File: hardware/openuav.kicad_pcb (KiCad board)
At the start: 4 copper layers, 36 x 36 mm, 80 parts, among them J1 Conn_01x01, J10 Conn_01x01, J11 Conn_01x01, J12 Conn_01x01, J13 Conn_01x01, J14 Conn_01x01, J15 Conn_01x01, J16 Conn_01x01, J17 Conn_01x01, J18 Conn_01x01, J19 Conn_01x01, J2 Conn_01x01, J20 Conn_01x01, J21 Conn_01x01, J22 Conn_01x01, J23 Conn_01x01, J24 Conn_01x01, J25 Conn_01x01, J3 Conn_01x01, J4 Conn_01x01, J5 Conn_01x01, J6 Conn_01x01, J7 Conn_01x01, J8 Conn_01x01, J9 Conn_01x01, J99 USB_C_Receptacle_USB2.0, SW1 SW_Push, U1 STM32G431CBUx, U2 LPS22HH, U3 LSM6DSR, U4 TPS54302, U5 TLV75733PDBV, U6 W25N01GVZEIG, U7 TLV75733PDBV

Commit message: Change IMU to ICM-42688-P. Change top and bottom planes to GND.
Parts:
- U3: value LSM6DSR -> ICM-42688-P
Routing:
- net GND: vias 51 -> 60
- added copper zone on B.Cu, net GND
- removed copper zone on B.Cu, net (none)
- removed copper zone on F.Cu, net (none)
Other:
- board text added: "OPENUAV v0.4"
- board text removed: "OPENUAV v0.3"
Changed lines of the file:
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@@
     (descr "LGA, 14 Pin (https://www.st.com/resource/en/datasheet/lsm6ds3tr-c.pdf), generated with kicad-footprint-generator ipc_noLead_generator.py")
     (tags "LGA NoLead")
-    (property "LCSC" "C784817")
+    (property "LCSC" "C1850418")
     (property "Sheetfile" "openuav.kicad_sch")
     (property "Sheetname" "")
@@
         (effects (font (size 1 1) (thickness 0.15)))
     )
-    (fp_text value "LSM6DSR" (at 39 -1) (layer "F.Fab")
+    (fp_text value "ICM-42688-P" (at 39 -1) (layer "F.Fab")
         (effects (font (size 1 1) (thickness 0.15)))
     )
@@
   (gr_arc locked (start 165 50) (mid 165.707107 50.292893) (end 166 51)
     (stroke (width 0.2) (type default)) (layer "Edge.Cuts"))
-  (gr_text "OPENUAV v0.3" (at 160 55) (layer "B.SilkS")
+  (gr_text "OPENUAV v0.4" (at 160.1 52.3) (layer "B.SilkS")
     (effects (font (size 1 1) (thickness 0.2) bold) (justify left bottom mirror))
   )
-  (gr_text "JLCJLCJLCJLC" (at 146 83) (layer "B.SilkS")
+  (gr_text "JLCJLCJLCJLC" (at 146.7 84.7) (layer "B.SilkS")
     (effects (font (size 1 1) (thickness 0.2) bold) (justify left bottom mirror))
   )
-  (gr_text "DFU" (at 132.9 79.1) (layer "F.SilkS")
+  (gr_text "DFU" (at 136 76.55 -90) (layer "F.SilkS")
     (effects (font (size 1 1) (thickness 0.2) bold))
   )
@@
   (via (at 152.522738 70.493202) (size 0.5) (drill 0.3) (layers "F.Cu" "B.Cu") (net 1))
   (via (at 142.9 72.7) (size 0.5) (drill 0.3) (layers "F.Cu" "B.Cu") (net 1))
+  (via (at 151.2 55.8) (size 0.5) (drill 0.3) (layers "F.Cu" "B.Cu") (free) (net 1))
   (via (at 152 76.4) (size 0.5) (drill 0.3) (layers "F.Cu" "B.Cu") (net 1))
+  (via (at 141.6 56.2) (size 0.5) (drill 0.3) (layers "F.Cu" "B.Cu") (free) (net 1))
+  (via (at 132.9 77.4) (size 0.5) (drill 0.3) (layers "F.Cu" "B.Cu") (free) (net 1))
   (via (at 137.523 61.1) (size 0.5) (drill 0.3) (layers "F.Cu" "B.Cu") (free) (net 1))
   (via (at 134.7 57.5) (size 0.5) (drill 0.3) (layers "F.Cu" "B.Cu") (net 1))
+  (via (at 142.6 77.3) (size 0.5) (drill 0.3) (layers "F.Cu" "B.Cu") (free) (net 1))
   (via (at 163.1 76.7) (size 0.5) (drill 0.3) (layers "F.Cu" "B.Cu") (net 1))
   (via (at 151.022738 70.493202) (size 0.5) (drill 0.3) (layers "F.Cu" "B.Cu") (net 1))
+  (via (at 164.7 67.9) (size 0.5) (drill 0.3) (layers "F.Cu" "B.Cu") (free) (net 1))
   (via (at 138.4 77) (size 0.5) (drill 0.3) (layers "F.Cu" "B.Cu") (net 1))
   (via (at 139.523 61.1) (size 0.5) (drill 0.3) (layers "F.Cu" "B.Cu") (free) (net 1))
   (via (at 138 53.4) (size 0.5) (drill 0.3) (layers "F.Cu" "B.Cu") (net 1))
+  (via (at 159.8 52.4) (size 0.5) (drill 0.3) (layers "F.Cu" "B.Cu") (free) (net 1))
   (via (at 151.922738 75.393202) (size 0.5) (drill 0.3) (layers "F.Cu" "B.Cu") (net 1))
   (via (at 153.222738 75.393202) (size 0.5) (drill 0.3) (layers "F.Cu" "B.Cu") (net 1))
   (via (at 151.022738 67.493202) (size 0.5) (drill 0.3) (layers "F.Cu" "B.Cu") (net 1))
+  (via (at 143.2 79.8) (size 0.5) (drill 0.3) (layers "F.Cu" "B.Cu") (free) (net 1))
   (via (at 152.522738 68.993202) (size 0.5) (drill 0.3) (layers "F.Cu" "B.Cu") (net 1))
   (via (at 149.522738 68.993202) (size 0.5) (drill 0.3) (layers "F.Cu" "B.Cu") (net 1))
@@
   (via (at 158 82.6) (size 0.5) (drill 0.3) (layers "F.Cu" "B.Cu") (net 1))
   (via (at 148 53.4) (size 0.5) (drill 0.3) (layers "F.Cu" "B.Cu") (net 1))
+  (via (at 154.3 80.5) (size 0.5) (drill 0.3) (layers "F.Cu" "B.Cu") (free) (net 1))
   (via (at 138.523 61.1) (size 0.5) (drill 0.3) (layers "F.Cu" "B.Cu") (free) (net 1))
   (via (at 138.5 81.3) (size 0.5) (drill 0.3) (layers "F.Cu" "B.Cu") (net 1))
@@
   (via (at 145.3 67.395) (size 0.5) (drill 0.3) (layers "F.Cu" "B.Cu") (net 1))
   (via (at 137.5 81.3) (size 0.5) (drill 0.3) (layers "F.Cu" "B.Cu") (net 1))
+  (via (at 148.2 84) (size 0.5) (drill 0.3) (layers "F.Cu" "B.Cu") (free) (net 1))
   (via (at 164.5 58.4) (size 0.5) (drill 0.3) (layers "F.Cu" "B.Cu") (net 1))
   (via (at 155.6 64.6) (size 0.5) (drill 0.3) (layers "F.Cu" "B.Cu") (net 1))
@@
   (segment (start 157.3 58.5) (end 157.2 58.6) (width 0.6) (layer "F.Cu") (net 4))
   (segment (start 157.3 56.7) (end 157.3 57.7) (width 0.2) (layer "F.Cu") (net 4))
-  (segment (start 145.8 58.175) (end 145.8 58.9) (width 0.6) (layer "F.Cu") (net 4))
   (segment (start 144.125 74.425) (end 145.325 74.425) (width 0.6) (layer "F.Cu") (net 4))
   (segment (start 148.735238 77.83094) (end 148.7475 77.843202) (width 0.6) (layer "F.Cu") (net 4))
   (segment (start 147.585238 65.730702) (end 147.585238 66.193202) (width 0.2) (layer "F.Cu") (net 4))
   (segment (start 148.272738 65.505702) (end 147.810238 65.505702) (width 0.2) (layer "F.Cu") (net 4))
+  (segment (start 145.8 58.175) (end 145.8 58.8) (width 0.6) (layer "F.Cu") (net 4))
   (segment (start 154.872738 57.753202) (end 155.932738 57.753202) (width 0.6) (layer "F.Cu") (net 4))
   (segment (start 148.75 77.193202) (end 148.75 77.840702) (width 0.2) (layer "F.Cu") (net 4))
@@
   (segment (start 155.672738 66.673202) (end 156.182738 66.163202) (width 0.2) (layer "F.Cu") (net 4))
   (segment (start 156.242738 75.85) (end 155.9 75.85) (width 0.6) (layer "F.Cu") (net 4))
-  (segment (start 145.8 58.9) (end 146.1 59.2) (width 0.6) (layer "F.Cu") (net 4))
   (segment (start 147.585238 66.193202) (end 146.462738 66.193202) (width 0.2) (layer "F.Cu") (net 4))
+  (segment (start 145.8 58.8) (end 146.2 59.2) (width 0.6) (layer "F.Cu") (net 4))
   (segment (start 155.652738 66.693202) (end 155.672738 66.673202) (width 0.2) (layer "F.Cu") (net 4))
   (segment (start 156.222738 74.8625) (end 156.222738 75.83) (width 0.2) (layer "F.Cu") (net 4))
@@
   (via (at 156.3 64) (size 0.5) (drill 0.3) (layers "F.Cu" "B.Cu") (net 4))
   (via (at 156 56.7) (size 0.5) (drill 0.3) (layers "F.Cu" "B.Cu") (net 4))
-  (via (at 146.1 59.2) (size 0.5) (drill 0.3) (layers "F.Cu" "B.Cu") (net 4))
+  (via (at 146.2 59.2) (size 0.5) (drill 0.3) (layers "F.Cu" "B.Cu") (net 4))
   (via (at 154.722738 75.393202) (size 0.5) (drill 0.3) (layers "F.Cu" "B.Cu") (net 4))
   (via (at 145.4 78.3) (size 0.5) (drill 0.3) (layers "F.Cu" "B.Cu") (net 4))
@@
     )
   )
-  (zone (net 0) (net_name "") (layers "F&B.Cu") (hatch edge 0.5)
-    (connect_pads no (clearance 0.25))
+  (zone (net 1) (net_name "GND") (layers "F&B.Cu") (hatch edge 0.5)
+    (connect_pads yes (clearance 0.25))
     (min_thickness 0.25) (filled_areas_thickness no)
-    (fill yes (thermal_gap 0.5) (thermal_bridge_width 0.5) (island_removal_mode 1) (island_area_min 10))
+    (fill yes (thermal_gap 0.5) (thermal_bridge_width 0.5))
     (polygon
       (pts

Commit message: PCB improvements
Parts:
- moved C23 1.57 mm to (147.4, 78.2), turned to -90 degrees
- moved C11 0.67 mm to (148.7, 77.7), turned to -90 degrees
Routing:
- net GND: track 70.6 -> 59.1 mm, vias 60 -> 59

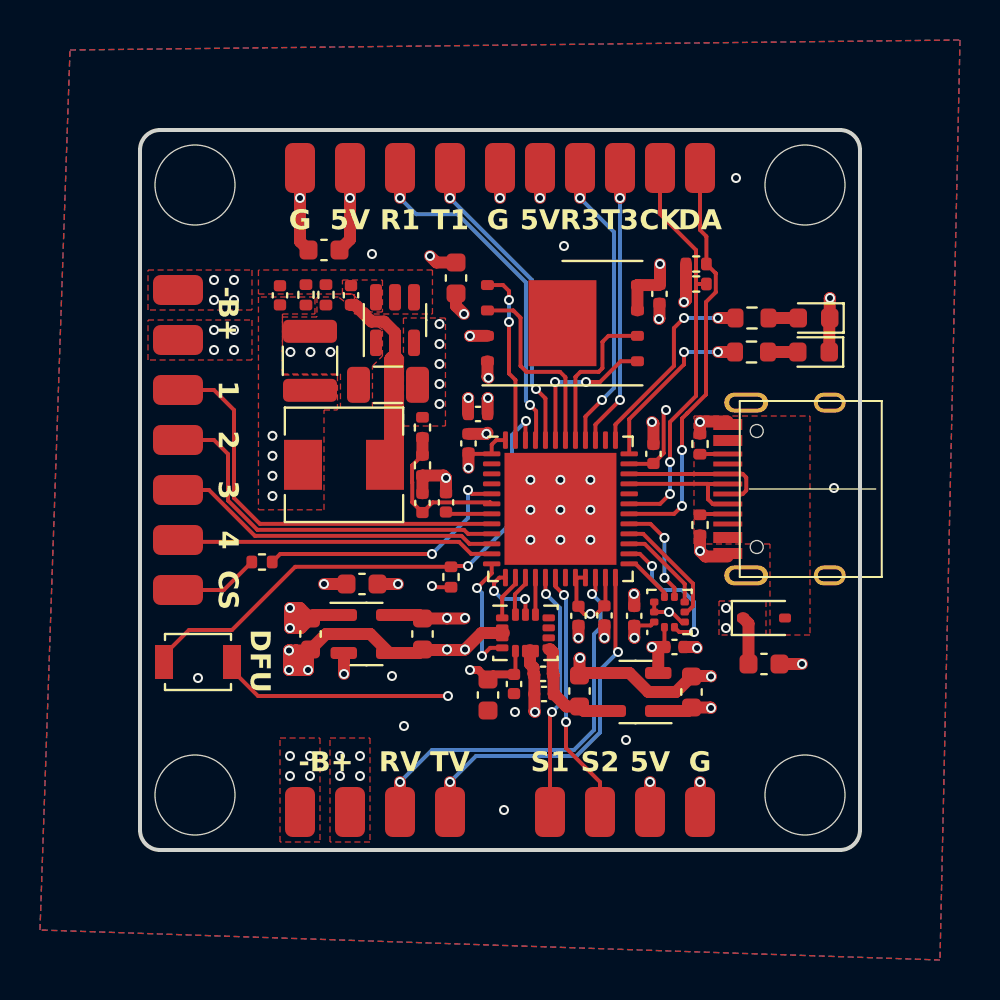
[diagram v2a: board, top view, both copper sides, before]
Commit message: Switch buck chip to LMR51420Y, add 9V SMPS.
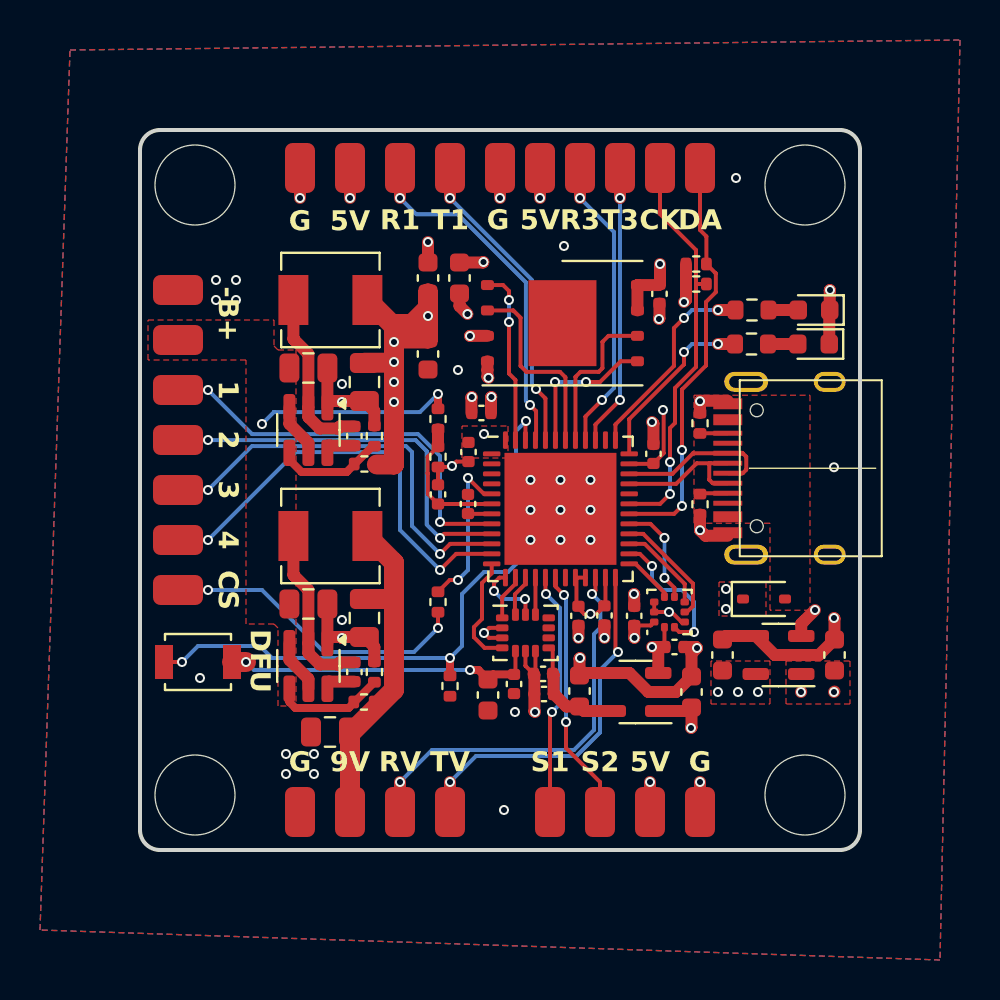
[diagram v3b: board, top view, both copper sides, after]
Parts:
- added C27: 100n, Capacitor_SMD:C_0402_1005Metric, F.Cu at (140.7, 77.1)
- added C28: 22u, Capacitor_SMD:C_0805_2012Metric, F.Cu at (141.2, 74.4)
- added L2: 6.8u, Inductor_SMD:L_Sunlord_MWSA0402S, F.Cu at (139.5, 70.3)
- added R13: 309k, Resistor_SMD:R_0402_1005Metric, F.Cu at (141.2, 78.6)
- added R14: 22.1k, Resistor_SMD:R_0402_1005Metric, F.Cu at (141.7, 77.1)
- added U8: ~, Package_TO_SOT_SMD:SOT-23-6, F.Cu at (138.4, 65.0)
- C10: value 68p -> 3.3u; footprint Capacitor_SMD:C_0402_1005Metric -> Capacitor_SMD:C_0805_2012Metric
- C15: value 47u -> 22u; footprint Capacitor_SMD:C_1210_3225Metric -> Capacitor_SMD:C_0805_2012Metric
- C2: value 10u -> 3.3u; footprint Capacitor_SMD:C_1206_3216Metric -> Capacitor_SMD:C_0805_2012Metric
- C20: value 10u -> 22u; footprint Capacitor_SMD:C_0603_1608Metric -> Capacitor_SMD:C_0805_2012Metric
- L1: value 10u -> 6.8u; footprint Inductor_SMD:L_Sunlord_MWSA0503S -> Inductor_SMD:L_Sunlord_MWSA0402S
- R3: value 100k -> 162k
- R4: value 13.3k -> 22.1k
- U4: value TPS54302 -> ~
- moved C17 26.2 mm to (164.7, 76.2), turned to 90 degrees
- moved C20 22.0 mm to (139.5, 80.1), turned to 180 degrees
- moved U7 20.6 mm to (161.9, 76.2), turned to 180 degrees
- moved U4 17.8 mm to (138.4, 76.8), turned to -90 degrees
- moved C22 15.7 mm to (144.4, 57.4), turned to 90 degrees
- moved C10 15.5 mm to (138.4, 73.7), turned to 0 degrees
- moved C8 15.0 mm to (159.1, 76.2), turned to 90 degrees
- moved R5 9.02 mm to (144.9, 73.6), turned to 90 degrees
- moved R3 8.95 mm to (141.2, 66.7), turned to 180 degrees
- moved L1 8.27 mm to (139.5, 58.5), turned to 0 degrees
- moved R4 7.46 mm to (141.7, 65.3), turned to 90 degrees
- moved C21 7.35 mm to (144.4, 61.2), turned to -90 degrees
- moved C9 7.04 mm to (140.7, 65.3)
- moved R8 5.45 mm to (145.5, 77.8)
- moved C2 4.07 mm to (138.4, 61.9), turned to 0 degrees
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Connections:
- C10 pad 1: Net-(U4-FB) -> +BATT
- C10 pad 2: +5V -> GND
- C20 pad 1: +5V -> +9V
- C9 pad 1: Net-(U4-BOOT) -> Net-(U8-SW)
- C9 pad 2: Net-(U4-SW) -> Net-(U8-CB)
- J10 pad 1: +BATT -> +9V
- L1 pad 1: Net-(U4-SW) -> Net-(U8-SW)
- R3 pad 2: Net-(U4-FB) -> Net-(U8-FB)
- R4 pad 1: Net-(U4-FB) -> Net-(U8-FB)
- U4 pad 5: unconnected-(U4-EN-Pad5) -> +BATT
- U4 pad 6: Net-(U4-BOOT) -> Net-(U4-CB)
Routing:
- net +9V: track 0.00 -> 16.8 mm
- net +BATT: track 27.5 -> 15.5 mm, vias 13 -> 2
- net CURRENT: track 4.27 -> 15.6 mm, vias 0 -> 2
- net +5V: track 20.9 -> 30.2 mm
- net Net-(U8-SW): track 0.00 -> 8.75 mm
- net +3V3: track 46.4 -> 39.8 mm, vias 14 -> 15
- net PWM_4: track 16.0 -> 22.4 mm, vias 0 -> 2
- net Net-(U4-FB): track 0.00 -> 5.57 mm
- net Net-(U8-FB): track 0.00 -> 5.39 mm
- net CSENSE: track 13.4 -> 8.07 mm
- net PWM_3: track 16.8 -> 21.2 mm, vias 0 -> 2
- net BOOT0: track 26.8 -> 30.9 mm, vias 2 -> 3
- net VOLTAGE: track 7.87 -> 6.54 mm
- net Net-(U8-CB): track 0.00 -> 1.31 mm
- net Net-(U4-CB): track 0.00 -> 1.31 mm
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- added copper zone on F.Cu, net +3V3
- removed copper zone on In1.Cu, net +BATT
- removed copper zone on F.Cu, net Net-(U4-BOOT)
- removed copper zone on F.Cu, net Net-(U4-FB)
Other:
- board text added: "9V"
- board text added: "OPENUAV v0.5"
- board text removed: "OPENUAV v0.4"

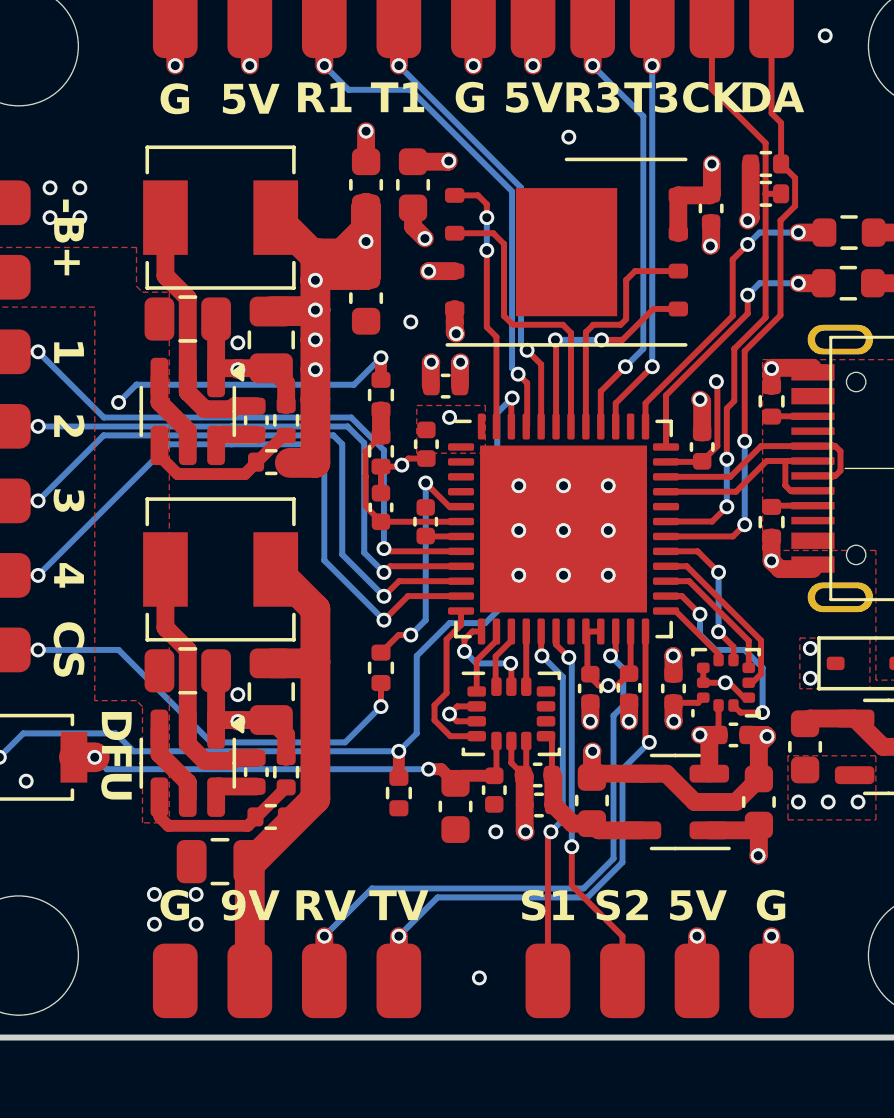
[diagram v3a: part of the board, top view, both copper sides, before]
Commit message: Minor layout improvements and part number changes
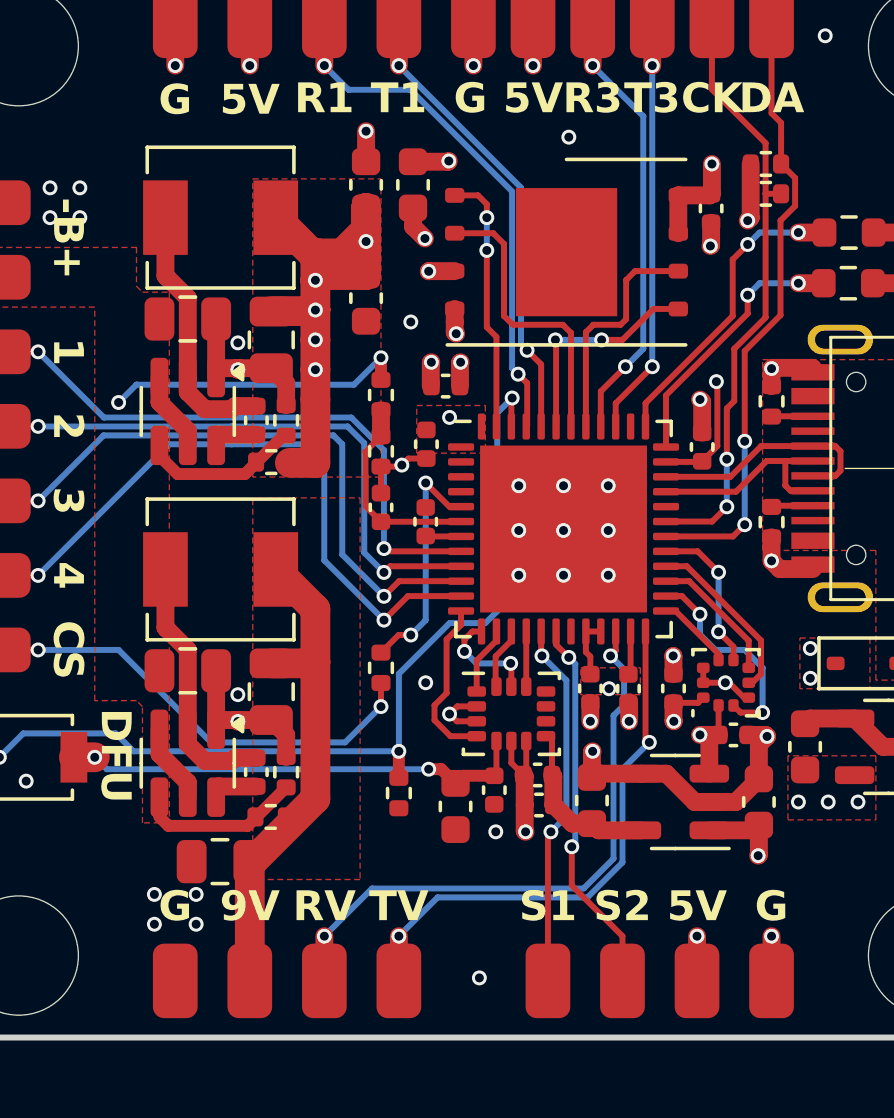
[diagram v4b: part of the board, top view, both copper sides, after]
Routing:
- net +3V3: track 39.8 -> 38.1 mm
- net GND: vias 50 -> 51
- added copper zone on F.Cu, net +9V
